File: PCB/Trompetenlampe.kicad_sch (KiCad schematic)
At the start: 6 parts, among them Q1 IRLZ44N, U1 TSR_1-2450, U2 ESP-12E

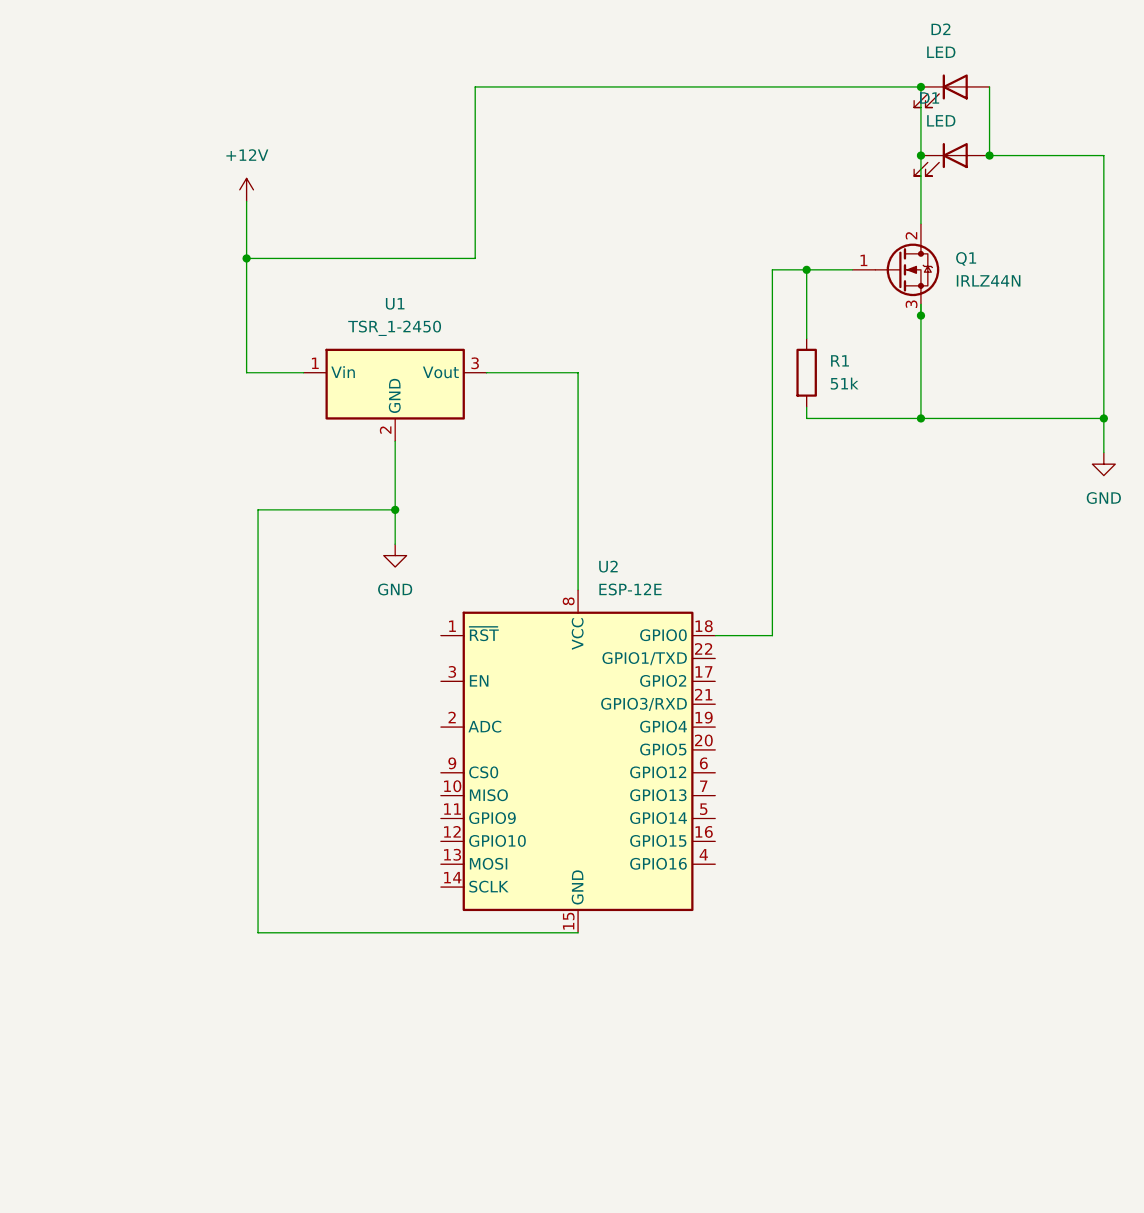
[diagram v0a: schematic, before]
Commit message: Corrected schematic
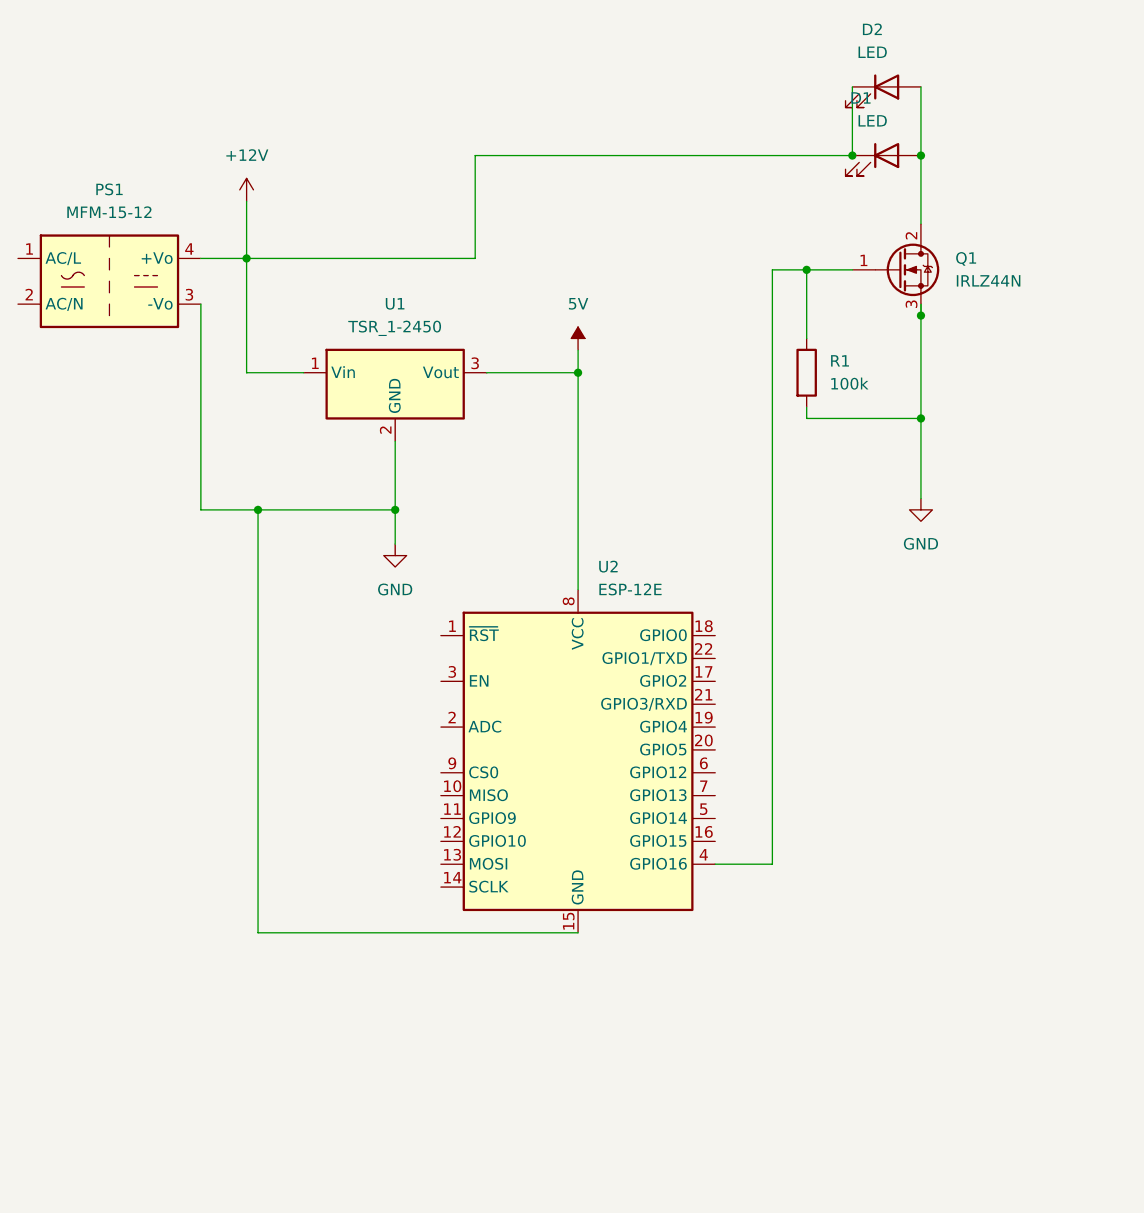
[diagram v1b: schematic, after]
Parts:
- added PS1: MFM-15-12, Converter_ACDC:Converter_ACDC_MeanWell_MFM-15-xx_THT, symbol Converter_ACDC:MFM-15-12
- R1: value 51k -> 100k
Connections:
- net +12V: now also PS1.4 (+Vo); no longer Q1.2 (D)
- net GND: now also PS1.3 (-Vo); no longer D1.2 (A), D2.2 (A)
- net 5V: now reaches U1.3 (Vout), U2.8 (VCC)
- net at Q1.1 (G), R1.1: now also U2.4 (GPIO16); no longer U2.18 (GPIO0)
- new net: D1.2 (A), D2.2 (A), Q1.2 (D)
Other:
- moved on the sheet: D1, D2

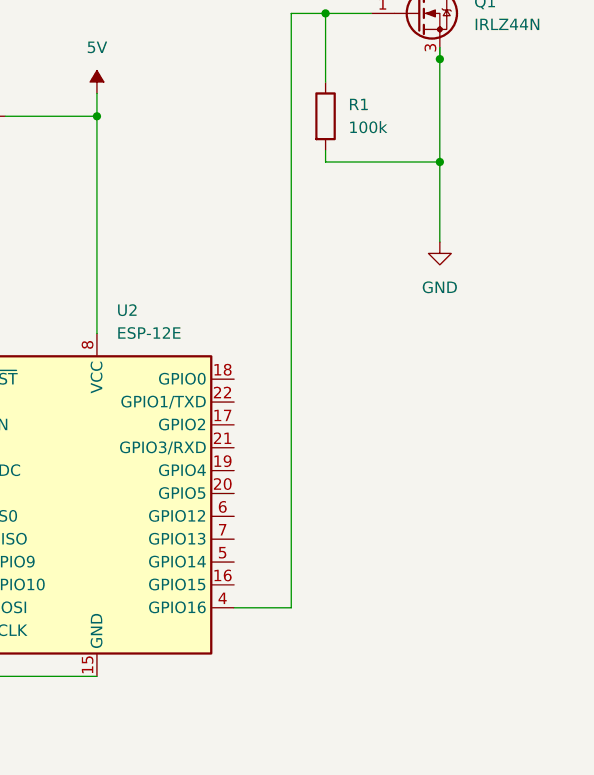
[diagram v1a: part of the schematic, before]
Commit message: Schematic extended. Rudimentary Software done. Holding Button is not working so far
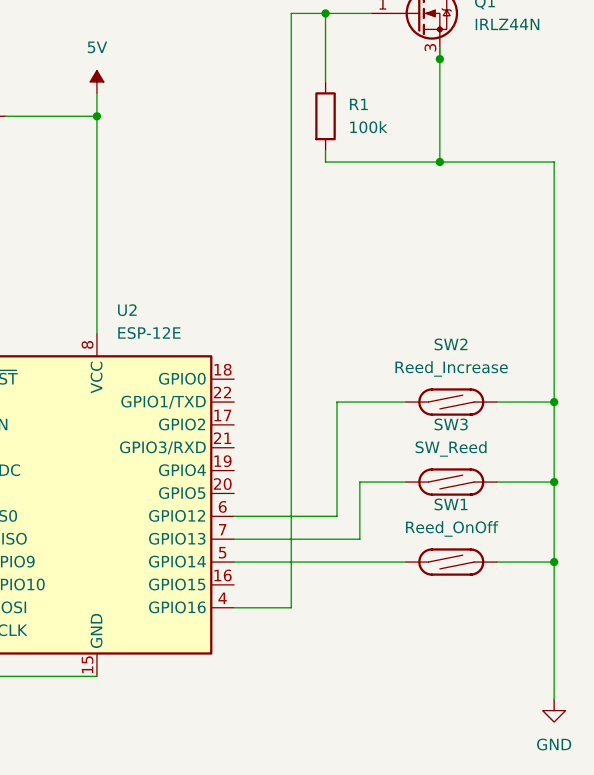
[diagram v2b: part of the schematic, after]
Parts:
- added SW1: Reed_OnOff, symbol Switch:SW_Reed
- added SW2: Reed_Increase, symbol Switch:SW_Reed
- added SW3: SW_Reed, symbol Switch:SW_Reed
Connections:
- net GND: now also SW1.2, SW2.2, SW3.2
- net at U2.5 (GPIO14): now also SW1.1
- net at U2.6 (GPIO12): now also SW2.1
- net at U2.7 (GPIO13): now also SW3.1

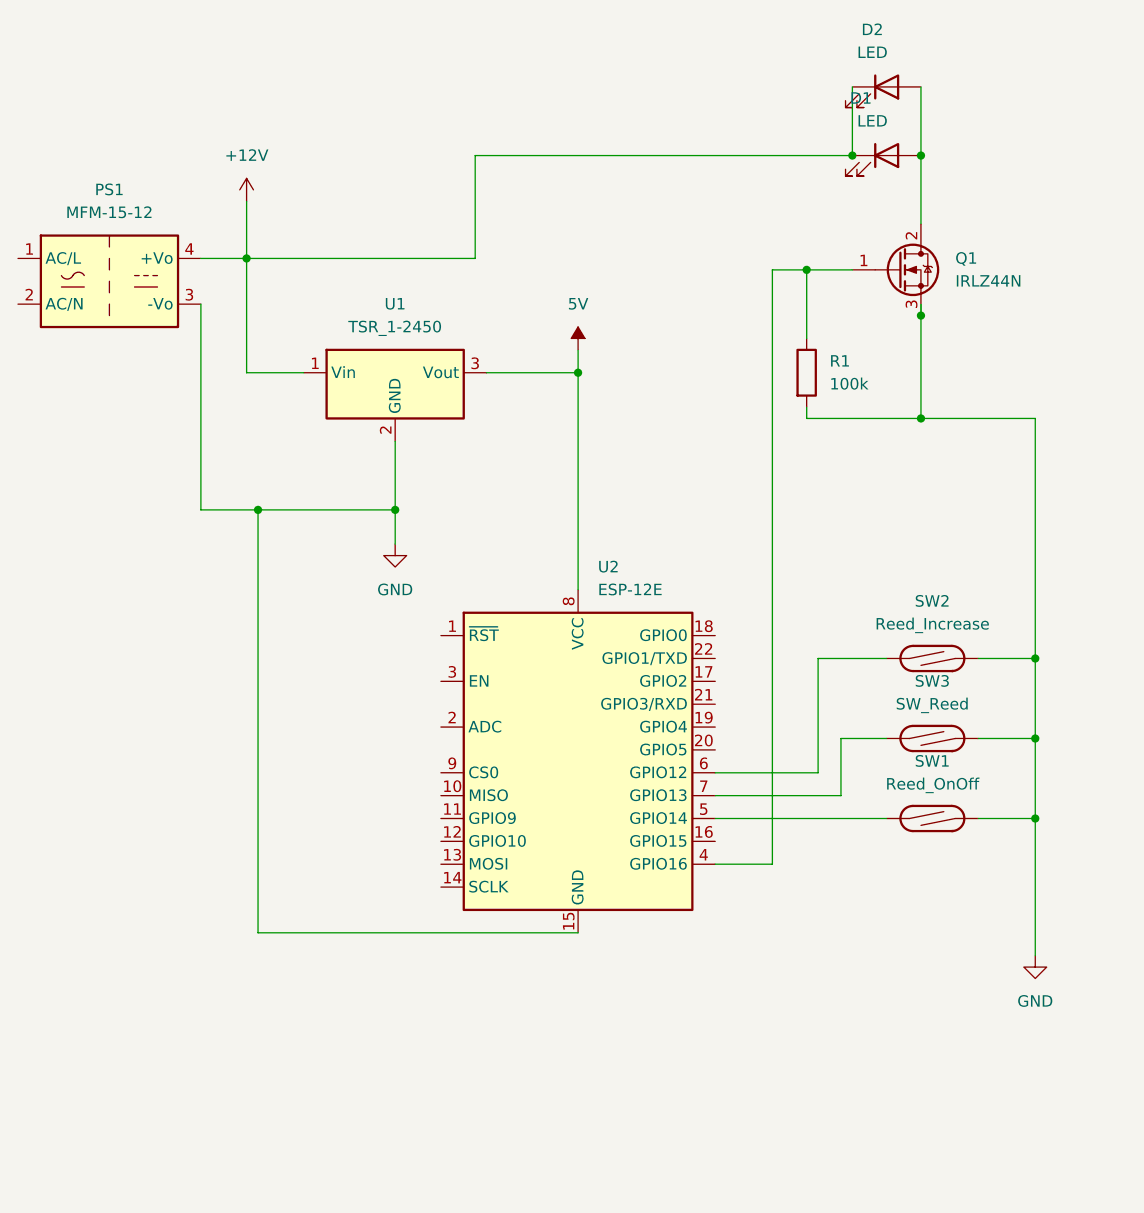
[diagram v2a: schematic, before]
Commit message: Changed uC to ESP32. Adjusted Circuit. Changed the code to work with either ESP32 or ESP8266
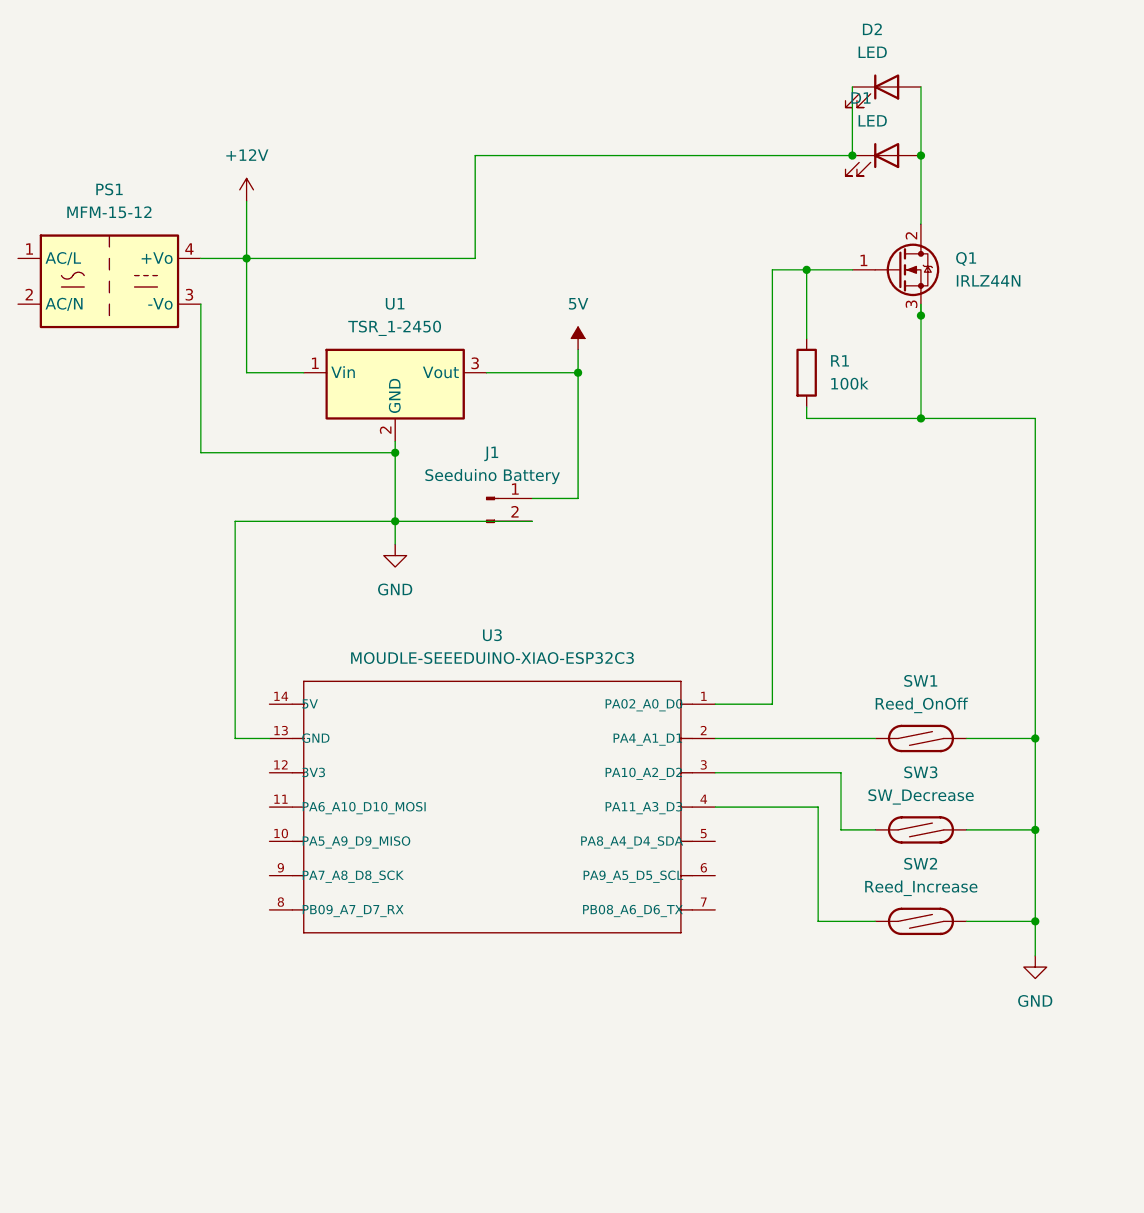
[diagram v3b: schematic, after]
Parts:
- removed U2: ESP-12E, RF_Module:ESP-12E, symbol RF_Module:ESP-12E
- added J1: Seeduino Battery, symbol Connector:Conn_01x02_Pin
- added U3: MOUDLE-SEEEDUINO-XIAO-ESP32C3, MOUDLE14P-SMD-2.54-21X17.8MM, symbol Seed ESP32:MOUDLE-SEEEDUINO-XIAO-ESP32C3
- SW3: value SW_Reed -> SW_Decrease
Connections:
- net 5V: now also J1.1 (Pin_1)
- net GND: now also J1.2 (Pin_2), U3.13 (GND)
- net at SW1.1: now also U3.2 (PA4_A1_D1)
- net at SW3.1: now also U3.3 (PA10_A2_D2)
- net at Q1.1 (G), R1.1: now also U3.1 (PA02_A0_D0)
- net at SW2.1: now also U3.4 (PA11_A3_D3)
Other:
- moved on the sheet: SW1, SW2, SW3

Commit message: updated the schematic
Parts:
- added R2, R3, R4: 5.1k, symbol Device:R
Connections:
- net at SW1.1, U3.2 (PA4_A1_D1): now also R2.1
- net at SW3.1, U3.3 (PA10_A2_D2): now also R3.1
- net at U3.12 (3V3): now also R2.2, R3.2, R4.2
- net at SW2.1, U3.4 (PA11_A3_D3): now also R4.1
